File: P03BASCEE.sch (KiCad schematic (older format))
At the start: 8 parts

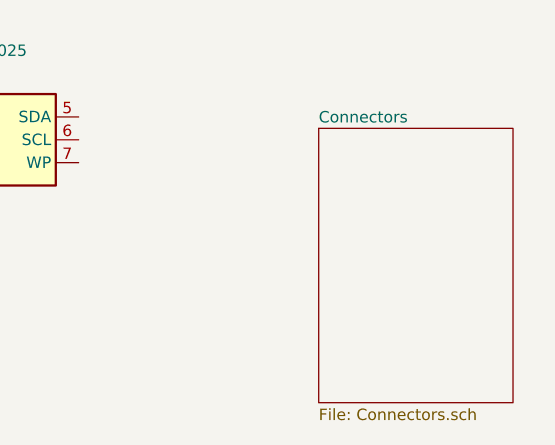
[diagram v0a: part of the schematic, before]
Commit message: Conectores colocados na página hierárquica correspondente
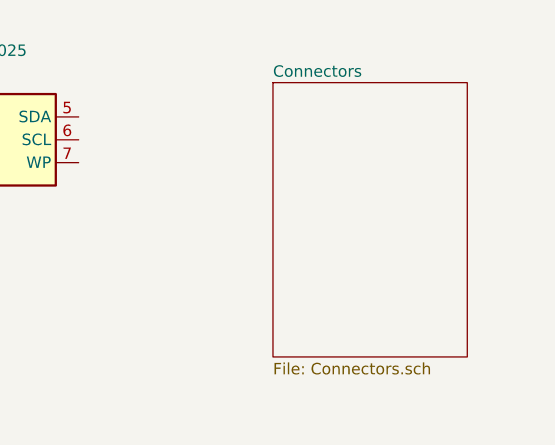
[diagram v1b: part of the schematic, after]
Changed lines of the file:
@@
 $Descr A4 11693 8268
 encoding utf-8
-Sheet 1 1
+Sheet 1 2
 Title "BASCEE "
 Date "2020-06-28"
@@
 $EndComp
 $Sheet
-S 8200 4050 850  1200
+S 8000 3850 850  1200
 U 5F03AF31
 F0 "Connectors" 50

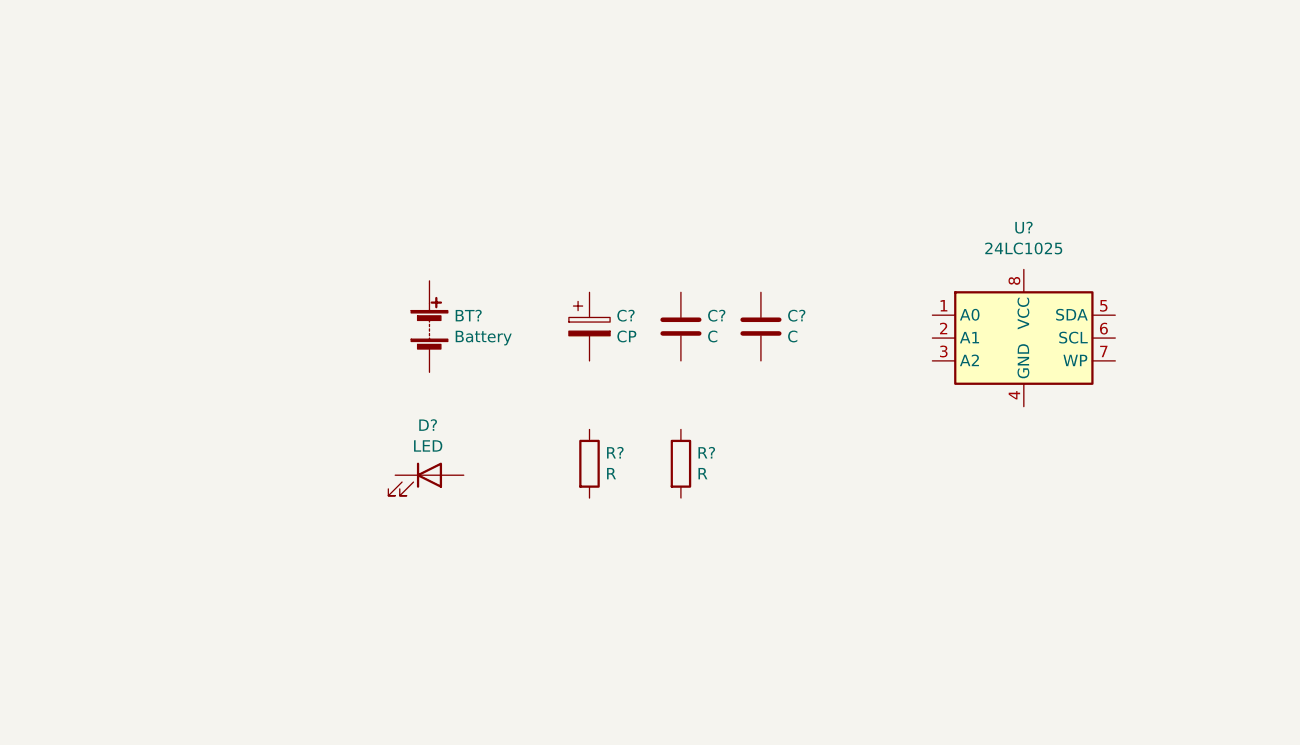
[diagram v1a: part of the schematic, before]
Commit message: Criado novo símbolo para CI e adicionado microcontrolador
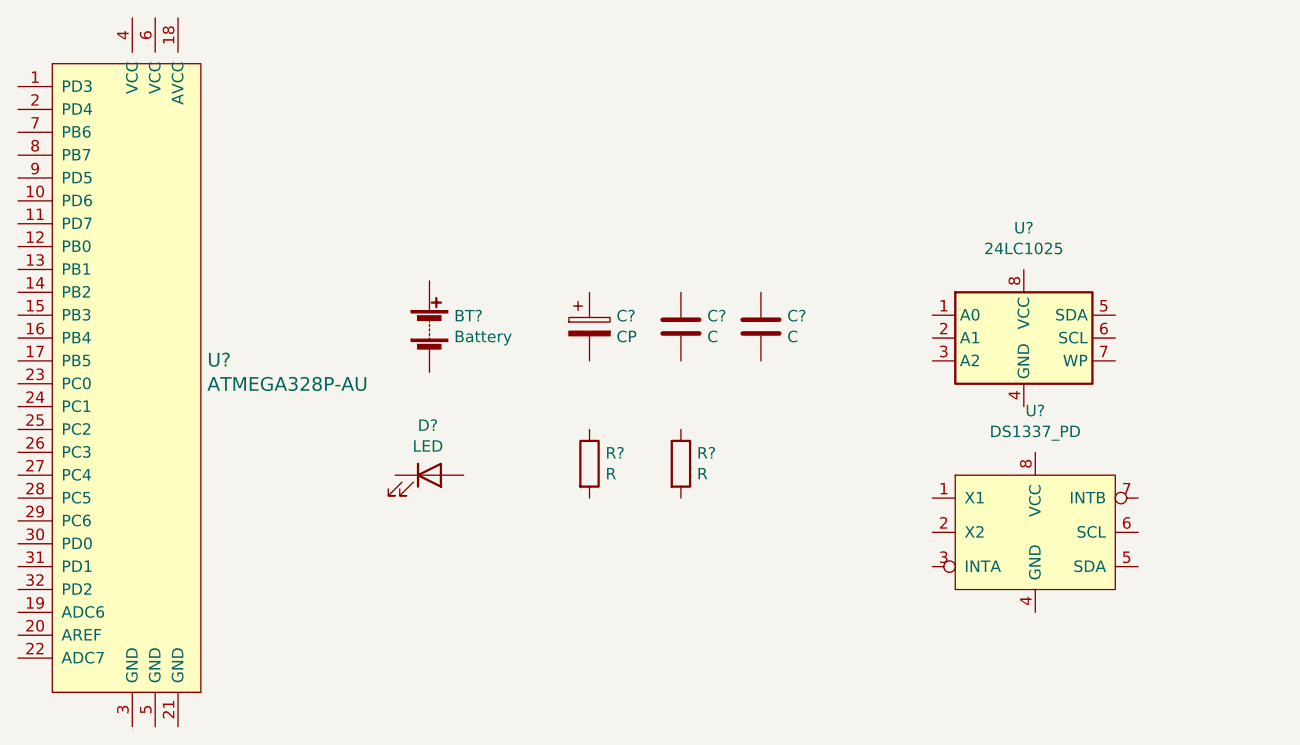
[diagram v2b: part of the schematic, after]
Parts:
- added U?: ATMEGA328P-AU, digikey-footprints:TQFP-32_7x7mm, symbol dk_Embedded-Microcontrollers:ATMEGA328P-AU
- added U?: DS1337_PD, symbol DS1337:DS1337_PD
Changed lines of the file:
@@
 F1 "Connectors.sch" 50
 $EndSheet
+$Comp
+L dk_Embedded-Microcontrollers:ATMEGA328P-AU U?
+U 1 1 5F040DB0
+P 2850 4300
+F 0 "U?" H 3178 4403 60  0000 L CNN
+F 1 "ATMEGA328P-AU" H 3178 4297 60  0000 L CNN
+F 2 "digikey-footprints:TQFP-32_7x7mm" H 3050 4500 60  0001 L CNN
+F 3 "http://www.microchip.com/mymicrochip/filehandler.aspx?ddocname=en608326" H 3050 4600 60  0001 L CNN
+F 4 "ATMEGA328P-AU-ND" H 3050 4700 60  0001 L CNN "Digi-Key_PN"
+F 5 "ATMEGA328P-AU" H 3050 4800 60  0001 L CNN "MPN"
+F 6 "Integrated Circuits (ICs)" H 3050 4900 60  0001 L CNN "Category"
+F 7 "Embedded - Microcontrollers" H 3050 5000 60  0001 L CNN "Family"
+F 8 "http://www.microchip.com/mymicrochip/filehandler.aspx?ddocname=en608326" H 3050 5100 60  0001 L CNN "DK_Datasheet_Link"
+F 9 "/product-detail/en/microchip-technology/ATMEGA328P-AU/ATMEGA328P-AU-ND/1832260" H 3050 5200 60  0001 L CNN "DK_Detail_Page"
+F 10 "IC MCU 8BIT 32KB FLASH 32TQFP" H 3050 5300 60  0001 L CNN "Description"
+F 11 "Microchip Technology" H 3050 5400 60  0001 L CNN "Manufacturer"
+F 12 "Active" H 3050 5500 60  0001 L CNN "Status"
+	1    2850 4300
+	1    0    0    -1
+$EndComp
+$Comp
+L DS1337:DS1337_PD U?
+U 1 1 5F04ABB9
+P 6800 4950
+F 0 "U?" H 6800 5481 50  0000 C CNN
+F 1 "DS1337_PD" H 6800 5390 50  0000 C CNN
+F 2 "" H 6800 5350 50  0001 C CNN
+F 3 "https://datasheets.maximintegrated.com/en/ds/DS1337-DS1337C.pdf" H 6800 5350 50  0001 C CNN
+	1    6800 4950
+	1    0    0    -1
+$EndComp
 $EndSCHEMATC

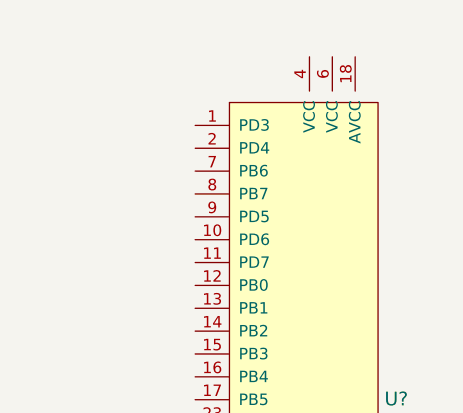
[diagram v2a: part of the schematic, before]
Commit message: Adicionados cristais que faltavam
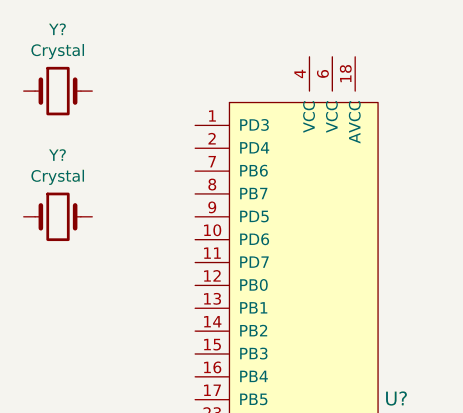
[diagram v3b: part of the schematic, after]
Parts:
- added Y? (x2): Crystal, symbol Device:Crystal
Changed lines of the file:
@@
+	1    0    0    -1
+$EndComp
+$Comp
+L Device:Crystal Y?
+U 1 1 5F04BC1B
+P 1750 2850
+F 0 "Y?" H 1750 3118 50  0000 C CNN
+F 1 "Crystal" H 1750 3027 50  0000 C CNN
+F 2 "" H 1750 2850 50  0001 C CNN
+F 3 "~" H 1750 2850 50  0001 C CNN
+	1    1750 2850
+	1    0    0    -1
+$EndComp
+$Comp
+L Device:Crystal Y?
+U 1 1 5F04CD00
+P 1750 3400
+F 0 "Y?" H 1750 3668 50  0000 C CNN
+F 1 "Crystal" H 1750 3577 50  0000 C CNN
+F 2 "" H 1750 3400 50  0001 C CNN
+F 3 "~" H 1750 3400 50  0001 C CNN
+	1    1750 3400
 	1    0    0    -1
 $EndComp
